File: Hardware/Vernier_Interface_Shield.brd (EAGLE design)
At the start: 76.2 x 78.7 mm, 44 parts, among them U1 74HC4052SO, U2 LMV358

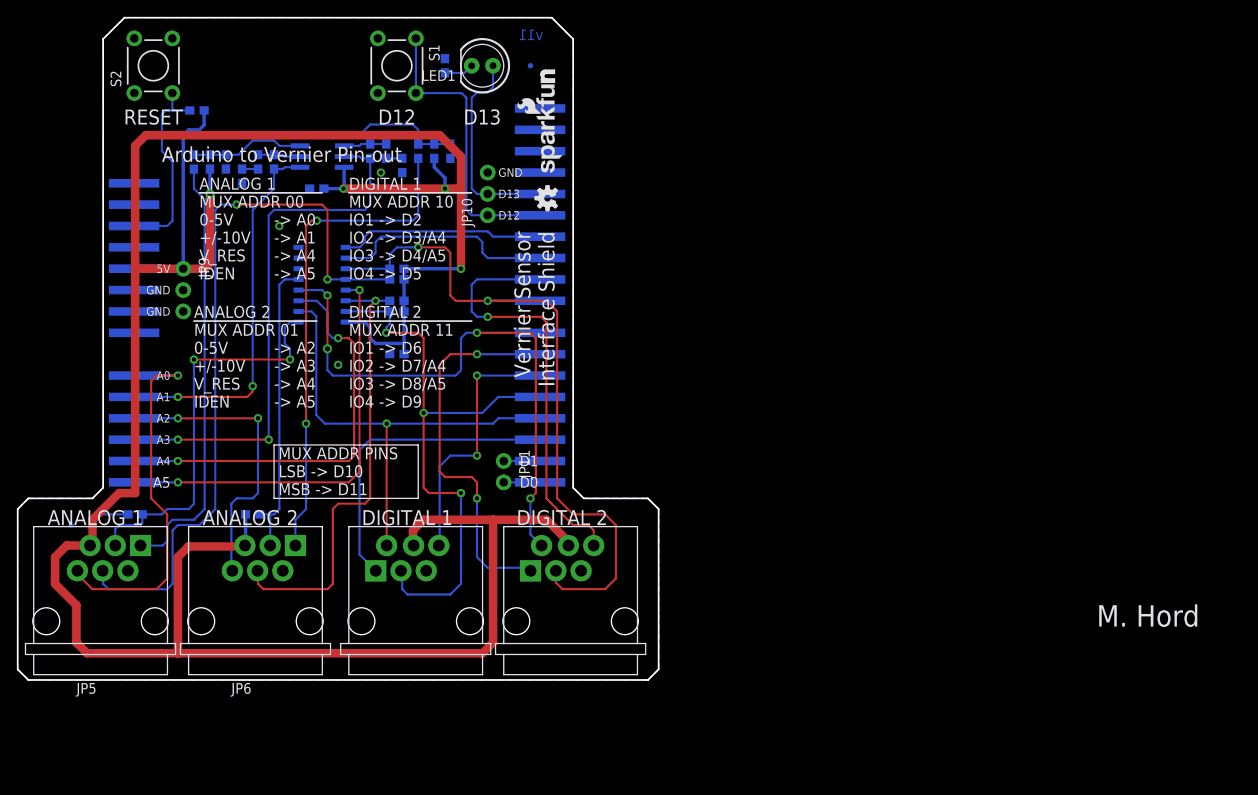
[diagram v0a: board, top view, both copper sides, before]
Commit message: Updated connector FPs. Tented some vias. Removed extra silk.
The A5 to A0 labels were of different size and didn't see to go
anywhere. Removed them.
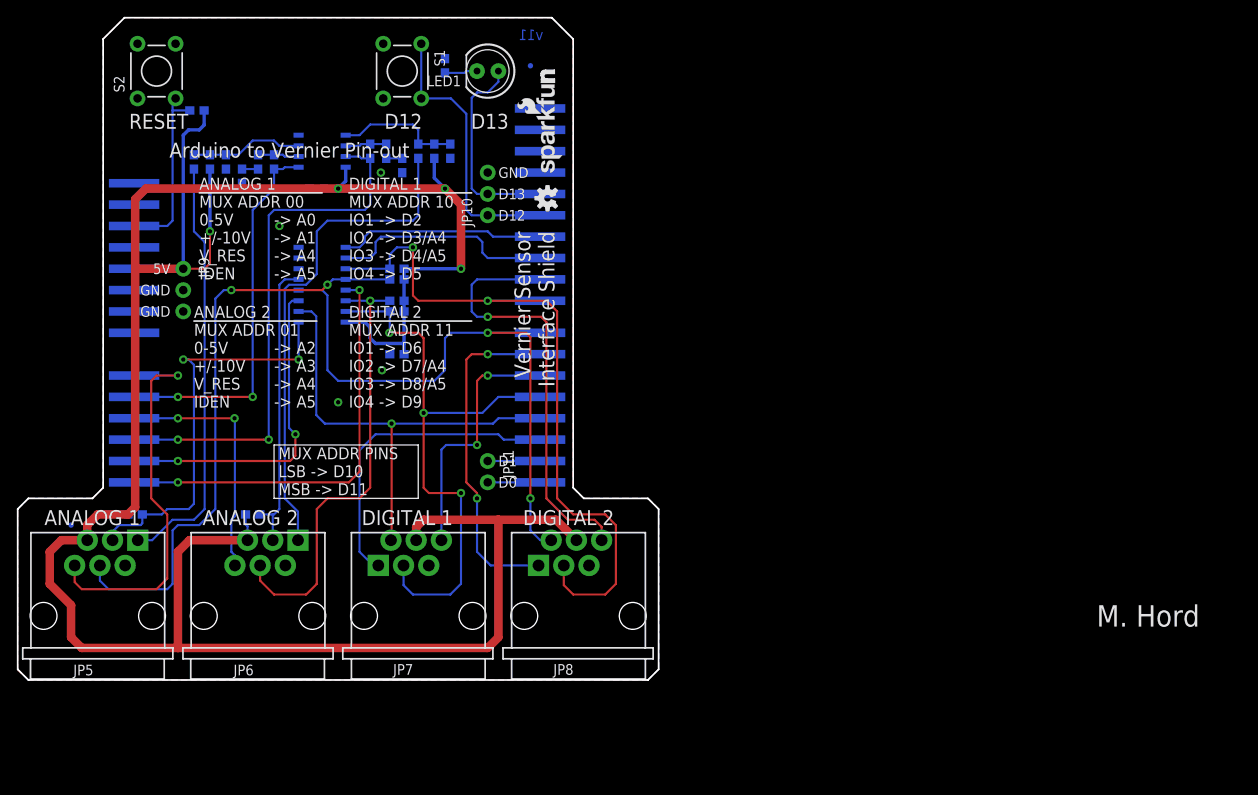
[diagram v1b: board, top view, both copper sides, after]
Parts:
- U2: value LMV358 -> LMV358SOICT; device SparkFun-AnalogIC:SO08 -> SparkFun-AnalogIC:SO08-TIGHT
- moved JP8 11.3 mm to (66.7, 7.62)
- moved JP7 10.8 mm to (47.6, 7.62)
- moved JP6 10.8 mm to (28.6, 7.62)
- moved JP5 10.3 mm to (9.53, 7.62)
- moved JP11 1.90 mm to (55.9, 26.0)
- moved LED1 0.90 mm to (55.9, 72.4)
- moved S1 0.90 mm to (45.7, 72.4)
- moved S2 0.74 mm to (16.5, 72.4)
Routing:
- net 5V: track 335.5 -> 308.5 mm
- net AS1_AUTOID: track 87.9 -> 70.3 mm
- net A4: track 50.0 -> 39.1 mm
- net D2_IO1: track 46.1 -> 40.4 mm
- net AS2_AN2: track 35.3 -> 29.8 mm
- net 12: track 35.1 -> 33.1 mm
- net RESET: track 23.6 -> 21.6 mm
- net 1: track 4.32 -> 6.22 mm
- net 0: track 4.32 -> 6.22 mm
- net AS1_AN2: track 45.3 -> 46.8 mm
- net AS1_VRES: track 47.7 -> 48.9 mm
- net D2_IO3: track 85.8 -> 86.9 mm
- net D2_IO2: track 75.3 -> 74.2 mm, vias 4 -> 2
- net AS1_AN1: track 51.5 -> 50.4 mm
- net D1_IO4: track 31.4 -> 30.6 mm
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
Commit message: Shrunk board. Updated version number to 1.2.
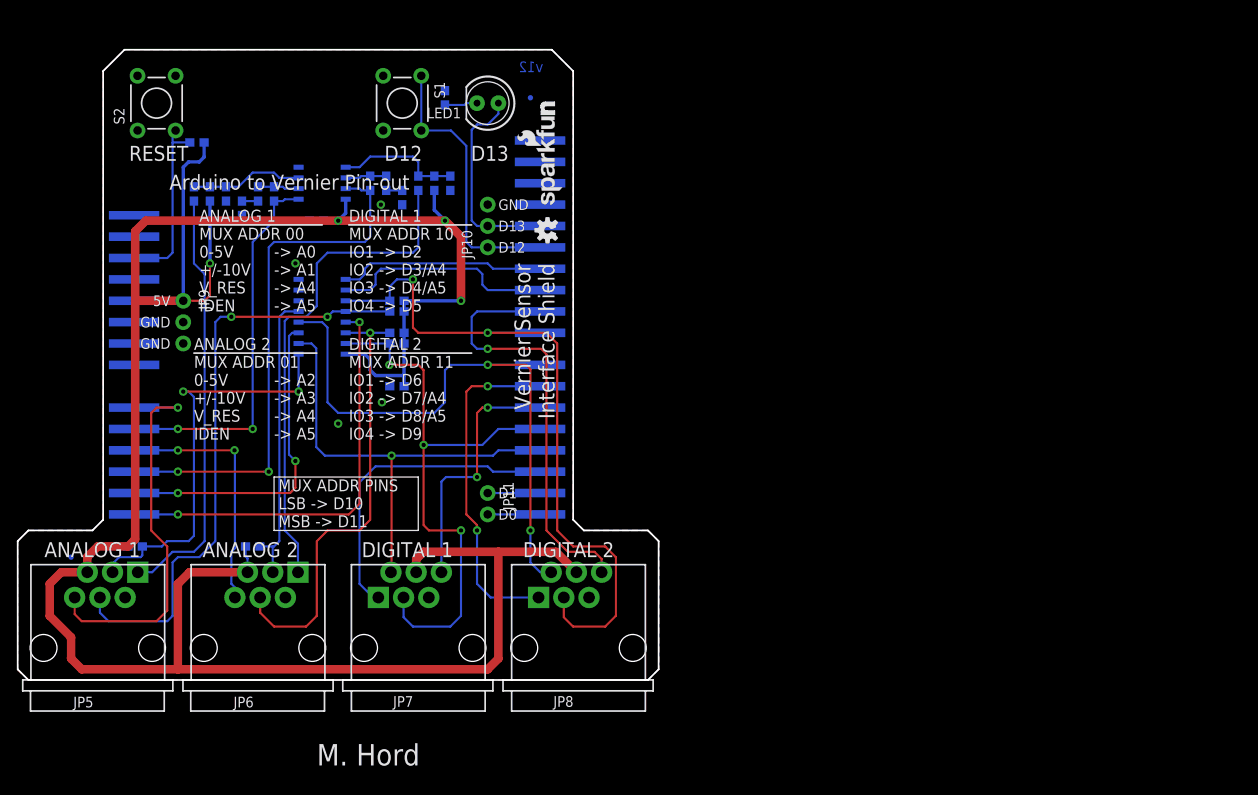
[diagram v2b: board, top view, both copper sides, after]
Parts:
- moved FRAME1 107.4 mm to (4.17, -10.2)
- moved C1 3.81 mm to (35.6, 54.6)
- moved C2 3.81 mm to (45.1, 34.9)
- moved FID2 3.81 mm to (61.0, 69.2)
- moved JP1 3.81 mm to (62.1, 41.3)
- moved JP2 3.81 mm to (62.1, 19.7)
- moved JP4 3.81 mm to (13.8, 19.7)
- moved JP9 3.81 mm to (19.7, 45.1)
- moved LED1 3.81 mm to (55.9, 68.6)
- moved LOGO2 3.81 mm to (63.0, 53.5)
- moved LOGO_1 3.81 mm to (62.2, 63.5)
- moved LOGO_3 3.81 mm to (64.8, 56.5)
- moved R1 3.81 mm to (24.8, 57.8)
- moved R10 3.81 mm to (43.8, 59.1)
- moved R11 3.81 mm to (41.9, 59.1)
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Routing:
- net 5V: track 308.5 -> 304.7 mm
- net AS1_AUTOID: track 70.3 -> 70.9 mm
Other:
- board size 76.2 x 78.7 mm -> 76.2 x 74.9 mm
- board text added: "v12"
- board text removed: "v11"

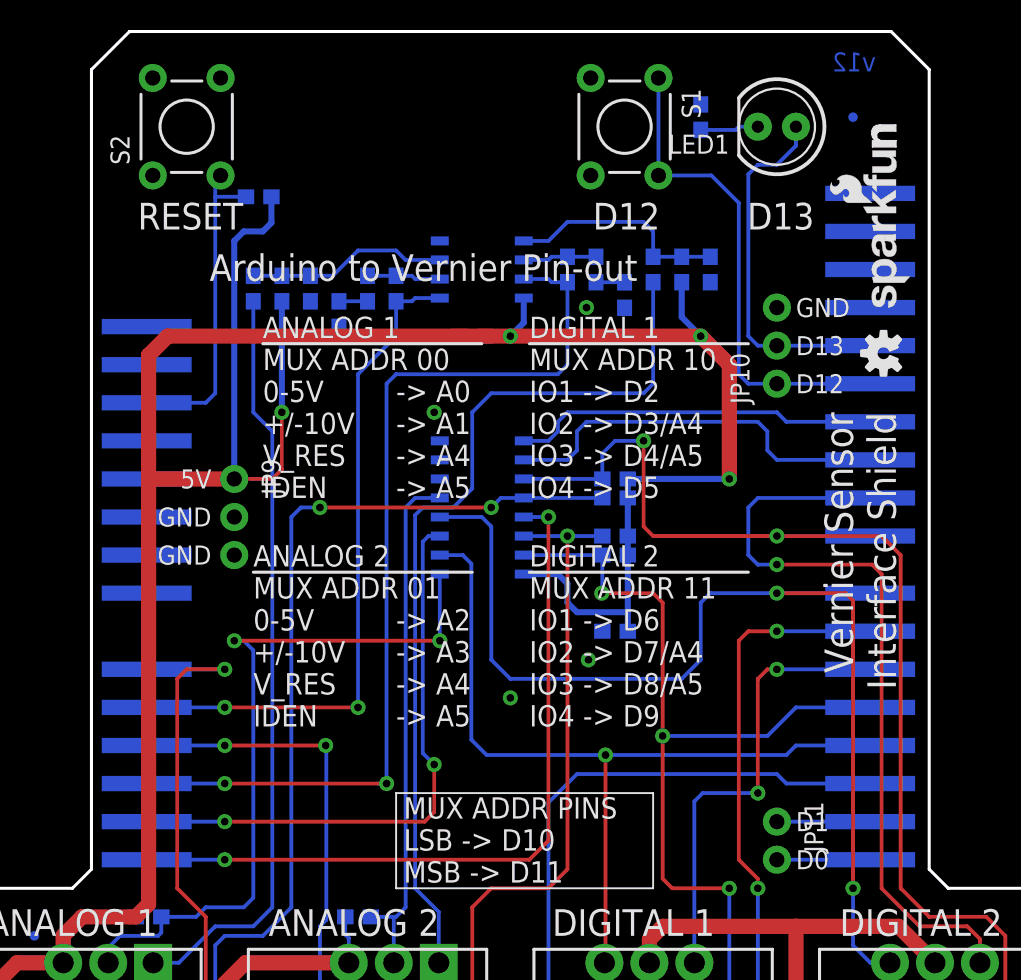
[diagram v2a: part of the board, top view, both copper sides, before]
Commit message: Touched up schematic. Updated version number.
Pushed some schematic components onto grid. Replaced button symbols with
single action symbol.
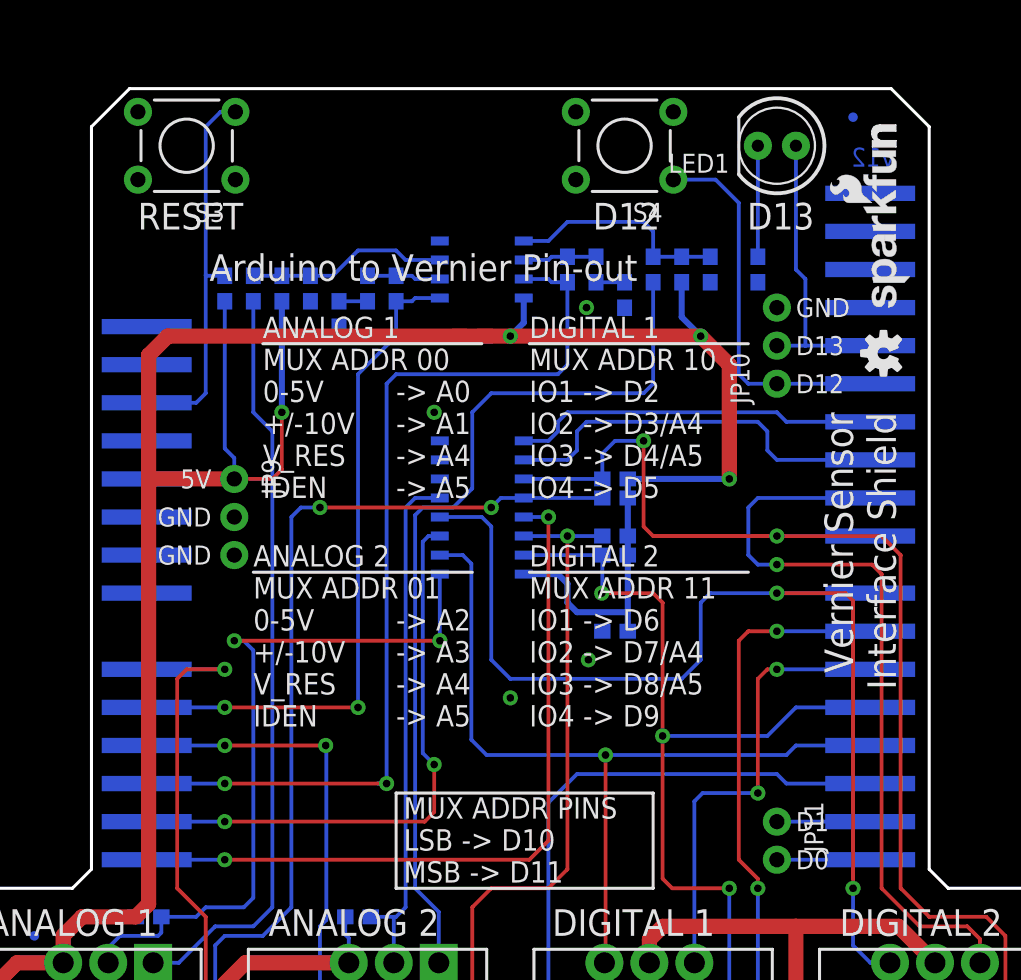
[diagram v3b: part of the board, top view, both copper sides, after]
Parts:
- removed S1, S2: (no value), SparkFun-Electromechanical:TACTILE-PTH
- added S3: Reset, SparkFun-Electromechanical:TACTILE-PTH
- added S4: D12, SparkFun-Electromechanical:TACTILE-PTH
- moved R19 10.9 mm to (54.6, 59.1), turned to 90 degrees
- moved R20 6.53 mm to (19.1, 57.8), turned to 270 degrees
- moved LED1 1.27 mm to (55.9, 67.3)
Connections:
- net 12: now also S4.1; no longer S1.1, S1.2
- net GND: now also S3.1, S4.3; no longer S1.3, S1.4, S2.1
- net RESET: now also S3.3; no longer S2.3
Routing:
- net 5V: track 304.7 -> 296.2 mm
- net 12: track 33.1 -> 25.5 mm
- net 13: track 24.4 -> 19.8 mm
- net RESET: track 21.6 -> 25.7 mm
- net N$9: track 3.90 -> 7.41 mm
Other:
- board size 76.2 x 74.9 mm -> 76.2 x 71.1 mm

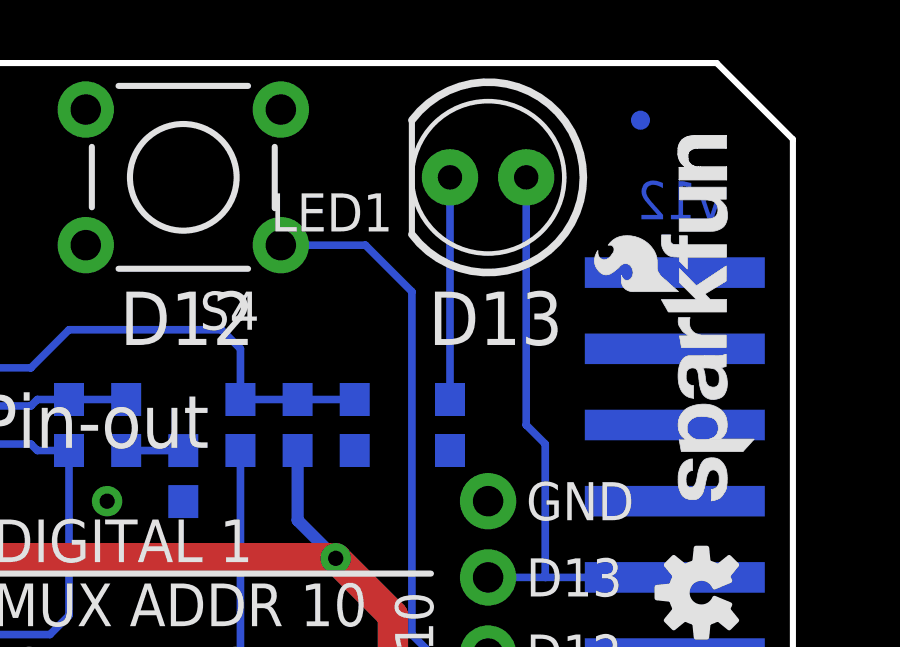
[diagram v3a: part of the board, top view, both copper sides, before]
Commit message: Small component/silk overlap fix.
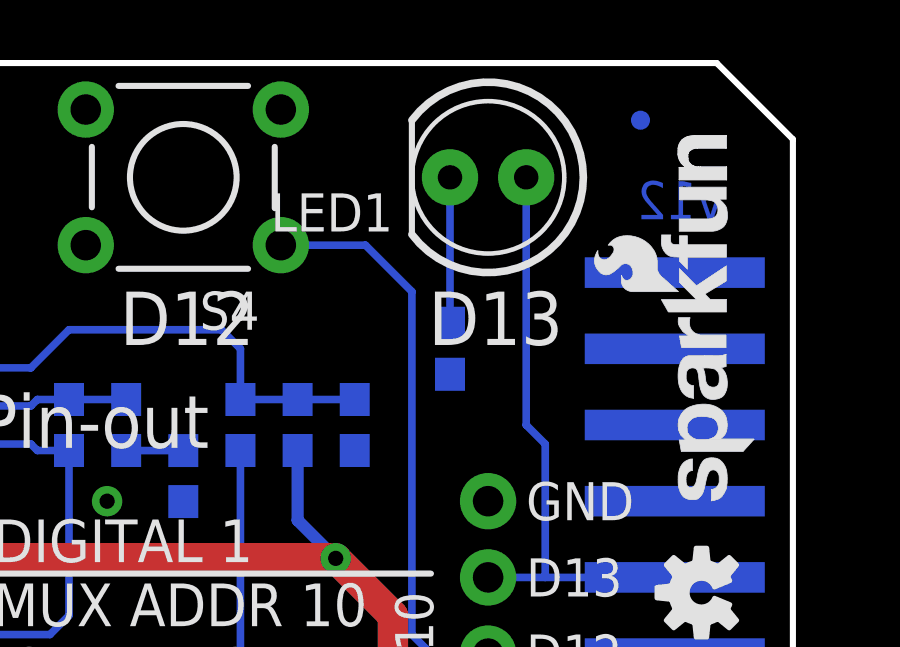
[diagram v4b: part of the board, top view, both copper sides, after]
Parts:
- moved R19 2.54 mm to (54.6, 61.6)
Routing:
- net N$9: track 7.41 -> 4.87 mm
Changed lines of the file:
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@@
 </element>
 <element name="LED1" library="SparkFun-LED" package="LED5MM" value="" x="55.88" y="67.31" rot="R180"/>
-<element name="R19" library="SparkFun-Resistors" package="0603-RES" value="330" x="54.61" y="59.055" rot="MR90">
-<attribute name="PROD_ID" value="RES-00818" x="54.61" y="59.055" size="1.778" layer="28" font="vector" ratio="15" rot="MR90" display="off"/>
+<element name="R19" library="SparkFun-Resistors" package="0603-RES" value="330" x="54.61" y="61.595" rot="MR90">
+<attribute name="PROD_ID" value="RES-00818" x="54.61" y="61.595" size="1.778" layer="28" font="vector" ratio="15" rot="MR90" display="off"/>
 </element>
 <element name="C1" library="SparkFun-Capacitors" package="0603-CAP" value="0.1uF" x="35.56" y="54.61" rot="MR0">
@@
 <contactref element="R19" pad="2"/>
 <contactref element="LED1" pad="K"/>
-<wire x1="54.61" y1="67.31" x2="54.61" y2="59.905" width="0.254" layer="16"/>
+<wire x1="54.61" y1="67.31" x2="54.61" y2="62.445" width="0.254" layer="16"/>
 </signal>
 <signal name="13">
